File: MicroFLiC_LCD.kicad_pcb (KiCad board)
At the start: 2 copper layers, 50 x 50 mm, 26 parts, among them P1 2x8 header strip, Q1 MJD31CT4G, U1 74AHCT367, U2 74AHCT367, U3 MCP4728, U4 TLV2371

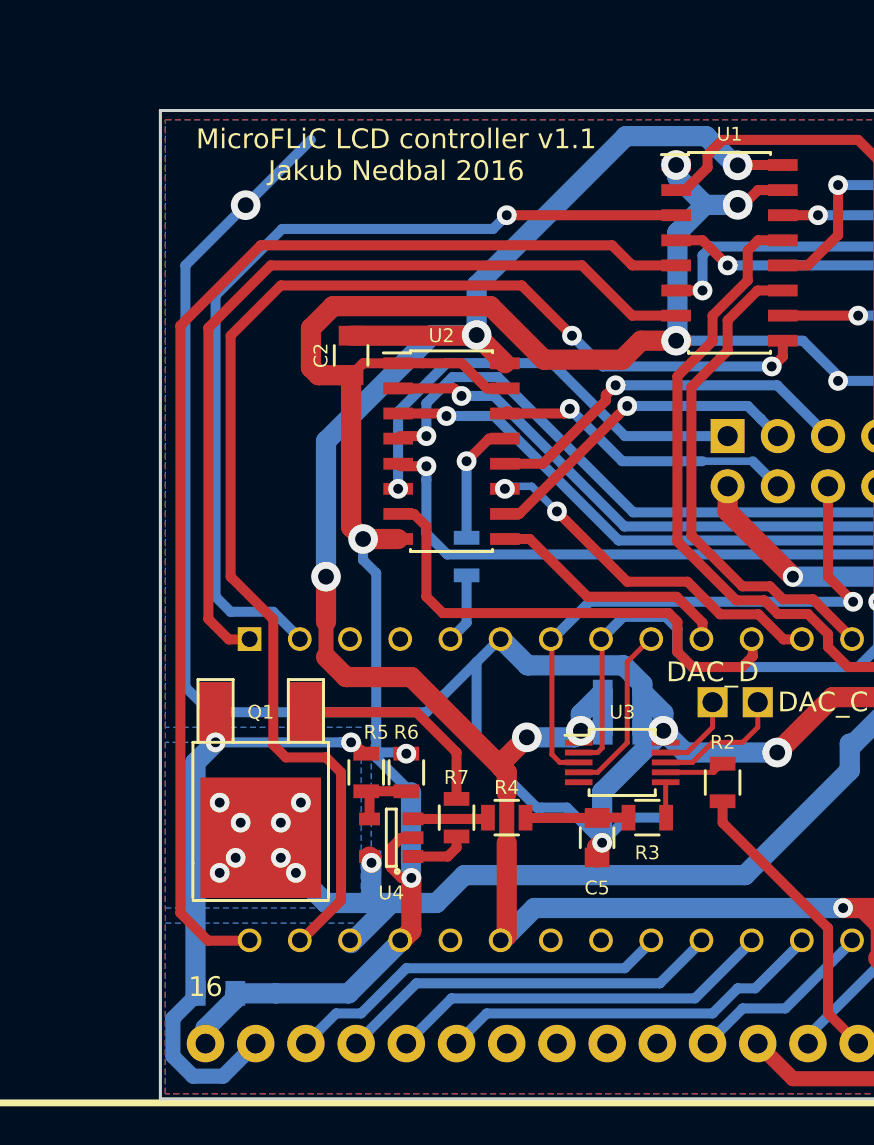
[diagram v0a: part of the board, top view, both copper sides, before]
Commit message: Added current-limiting resistors on the LCD backlight
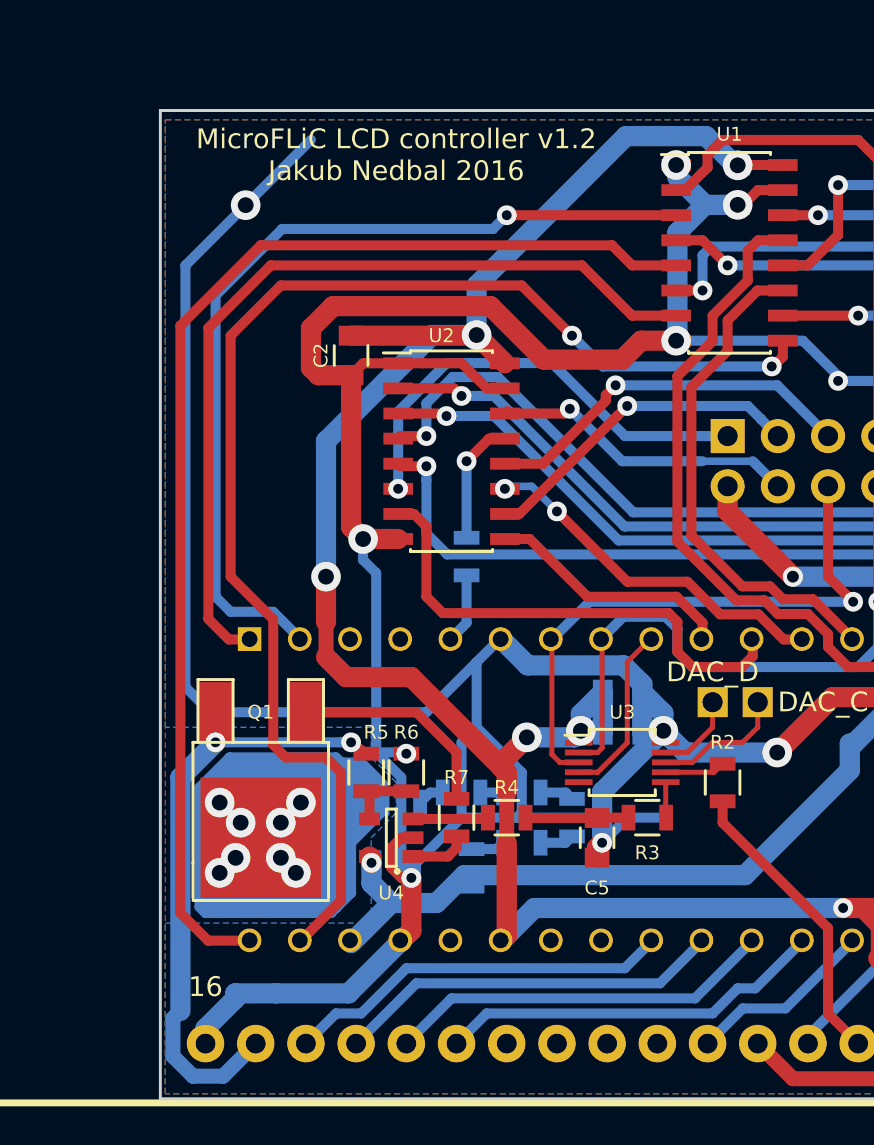
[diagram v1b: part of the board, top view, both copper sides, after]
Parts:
- removed C7: 4u7/25V, Capacitors_SMD:C_0805
- added R10: 6R8, Resistors_SMD:R_0805, B.Cu at (100.6, 144.8)
- added R11: 6R8, Resistors_SMD:R_0805, B.Cu at (103.1, 146.1)
- added R12: 6R8, Resistors_SMD:R_0805, B.Cu at (100.6, 147.3)
- added R13: 6R8, Resistors_SMD:R_0805, B.Cu at (98.0, 148.6)
- added R8: 6R8, Resistors_SMD:R_0805, B.Cu at (94.5, 145.3)
- added R9: 6R8, Resistors_SMD:R_0805, B.Cu at (97.5, 144.8)
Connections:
- Q1 pad 2: +12V -> Net-(Q1-Pad2)
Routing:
- net Net-(Q1-Pad2): track 0.00 -> 140.4 mm, vias 0 -> 8
- net +12V: track 86.4 -> 55.8 mm, vias 10 -> 2
- net GND: track 268.8 -> 281.5 mm
- net Net-(R12-Pad1): track 0.00 -> 1.72 mm
- net Net-(R11-Pad1): track 0.00 -> 1.72 mm
- net Net-(R10-Pad1): track 0.00 -> 1.72 mm
- net Net-(R8-Pad1): track 0.00 -> 1.36 mm
- net Net-(R10-Pad2): track 0.00 -> 1.15 mm
- removed copper zone on B.Cu, net +12V
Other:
- board text added: "MicroFLiC LCD controller v1.2 Jakub Nedbal 2016"
- board text removed: "MicroFLiC LCD controller v1.1 Jakub Nedbal 2016"

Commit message: Changed resistors on the PCB
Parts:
- R2: value 10k -> 47R
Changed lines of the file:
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@@
   )
   (setup
-    (last_trace_width 1.024)
+    (last_trace_width 0.254)
     (user_trace_width 0.254)
     (user_trace_width 0.381)
@@
       (effects (font (size 0.7 0.7) (thickness 0.11)))
     )
-    (fp_text value 10k (at 0 2.1 90) (layer F.Fab) hide
+    (fp_text value 47R (at 0 2.1 90) (layer F.Fab) hide
       (effects (font (size 1 1) (thickness 0.15)))
     )
